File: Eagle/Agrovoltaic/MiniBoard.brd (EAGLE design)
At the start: 199.4 x 149.9 mm, 88 parts, among them J1 WAGO-03BE, J2 WAGO-03BE, J3 WAGO-03BE, K1 SRD-05VDC-SL-C, K3 SRD-05VDC-SL-C, Q1 BC338, Q2 BC338, U1 ESP32-DEVKIT-V1

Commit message: Revisi lagiii
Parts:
- removed LNC1, LNC2: (no value), led_WS:LED3MM
- removed R10, R15, R16, R9: (no value), rcl-ws:0309/12
- added A1: LM35DZ/NOPB, LM35DZ_NOPB:TO92127P521H735-3
- added PAD1, PAD10, PAD100, PAD101, PAD102, PAD103, PAD104, PAD11, PAD12, PAD13, PAD14, PAD15, PAD16, PAD17, PAD18, PAD19, PAD2, PAD20, PAD21, PAD22, PAD23, PAD24, PAD25, PAD26, PAD27, PAD28, PAD29, PAD3, PAD30, PAD31, PAD32, PAD33, PAD34, PAD35, PAD36, PAD37, PAD38, PAD39, PAD4, PAD40, PAD41, PAD42, PAD43, PAD44, PAD45, PAD46, PAD47, PAD48, PAD49, PAD5, PAD50, PAD51, PAD52, PAD53, PAD54, PAD55, PAD56, PAD57, PAD58, PAD59, PAD6, PAD60, PAD61, PAD62, PAD63, PAD64, PAD65, PAD66, PAD67, PAD68, PAD69, PAD7, PAD70, PAD71, PAD72, PAD73, PAD74, PAD75, PAD76, PAD77, PAD78, PAD79, PAD8, PAD80, PAD81, PAD82, PAD83, PAD84, PAD85, PAD86, PAD87, PAD88, PAD89, PAD9, PAD90, PAD91, PAD92, PAD93, PAD94, PAD95, PAD96, PAD97, PAD98, PAD99: WIREPAD1,6/0,9, wirepad-ws:1,6/0,9
- added RLM35: (no value), rcl-ws:0309/12
- moved R5 41.4 mm to (36.2, 125.6), turned to 90 degrees
- moved R3 41.1 mm to (5.97, 125.7), turned to 270 degrees
- moved RL5 2.62 mm to (193.7, 16.5)
- moved R4 2.07 mm to (60.6, 94.5)
- moved OLED_LCD 1.27 mm to (99.1, 63.5)
- moved R25 0.51 mm to (135.9, 99.8), turned to 180 degrees
- moved LNO1 0.51 mm to (7.62, 142.7), turned to 180 degrees
- moved LNO2 0.51 mm to (39.4, 142.7)
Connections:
- removed net N$11: LNC2.K, R16.1
- removed net N$13: LNC1.K, R10.1
- net 5V: now also A1.1
- net D25: now also A1.2, RLM35.2
- net GND: now also A1.3, R5.1, RLM35.1; no longer R10.2, R15.2, R16.2, R5.2, R9.2
- net N$10: now also R5.2; no longer R15.1
- net N$12: now also R3.1; no longer R9.1
- net N$3: now also LNO1.A; no longer R3.1
- net N$6: now also LNO2.A; no longer R5.1
- net NC1: no longer LNC1.A
- net NC2: no longer LNC2.A
- net NO1: no longer LNO1.A
- net NO2: no longer LNO2.A
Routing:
- net GND: track 1166.8 -> 1234.5 mm, vias 15 -> 12
- net N$6: track 35.4 -> 84.2 mm
- net S1: track 124.7 -> 165.1 mm
- net N$3: track 38.7 -> 60.6 mm
- net 5V: track 615.3 -> 593.7 mm, vias 8 -> 6
- net OUT1: track 32.7 -> 50.1 mm
- net D25: track 13.4 -> 26.8 mm
- net N$31: track 0.00 -> 12.3 mm
- net N$30: track 0.00 -> 12.3 mm
- net N$12: track 0.00 -> 11.7 mm
- net N$10: track 0.00 -> 11.6 mm
- net A1: track 208.2 -> 203.0 mm, vias 4 -> 3
- net OUT2: track 31.2 -> 35.9 mm
- net NC2: track 34.9 -> 30.5 mm
- net SCL: track 122.9 -> 126.4 mm
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
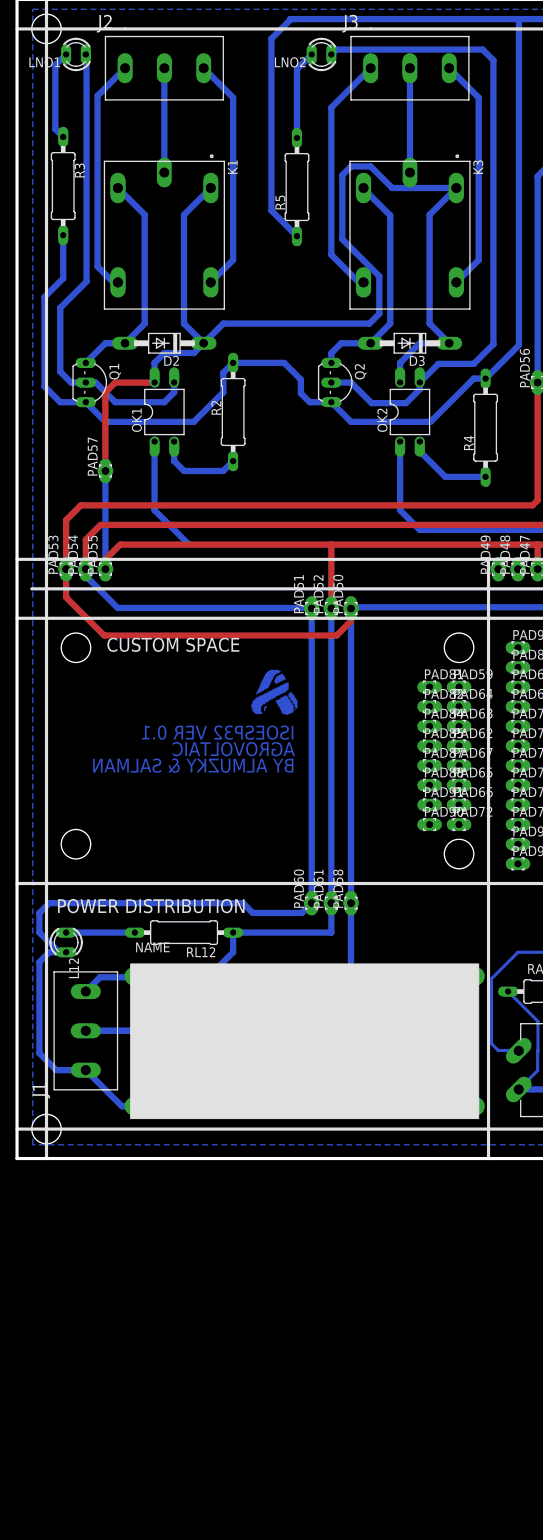
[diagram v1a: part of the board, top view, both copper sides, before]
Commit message: Revisi lagi lamp ke colector relay
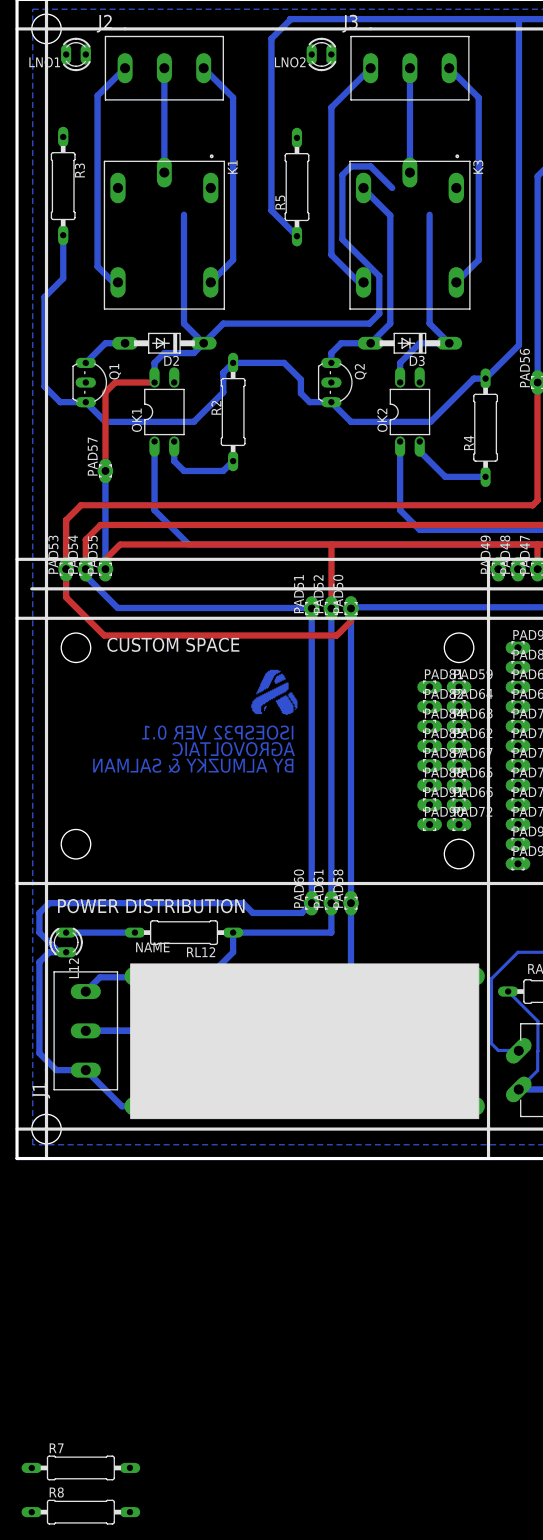
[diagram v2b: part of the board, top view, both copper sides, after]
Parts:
- added R7, R8: 2K, rcl-ws:0309/12
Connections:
- removed net N$12: LNO1.K, R3.1
- new net N$11: D2.A, K1.A2, LNO1.K, Q1.C
- net 12V: now also R7.1, R8.1
- net N$10: now also LNO1.A, R8.2; no longer LNO2.K, R5.2
- net N$3: now also R3.1; no longer LNO1.A
- net N$4: now also D3.A, K3.A2, LNO2.K, Q2.C; no longer D2.A, K1.A2, Q1.C
- net N$6: now also R5.2; no longer LNO2.A
- net N$7: now also LNO2.A, R7.2; no longer D3.A, K3.A2, Q2.C
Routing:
- net N$6: track 84.2 -> 0.00 mm
- net N$3: track 60.6 -> 0.00 mm
- net N$7: track 29.4 -> 0.00 mm
- net 12V: track 477.7 -> 459.6 mm
- net N$12: track 11.7 -> 0.00 mm
- net N$10: track 11.6 -> 0.00 mm
- net N$11: track 0.00 -> 6.13 mm
- net N$4: track 28.7 -> 29.3 mm

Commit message: Revisi board dan revisi wiring diagram
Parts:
- moved R8 178.1 mm to (19.1, 132.1), turned to 180 degrees
- moved R7 177.3 mm to (50.8, 132.1), turned to 180 degrees
- moved RA13 2.54 mm to (96.5, 110.5)
- moved R3 2.13 mm to (8.00, 125.1), turned to 90 degrees
- moved RA12 1.91 mm to (96.5, 117.5)
- moved RA22 1.91 mm to (76.2, 117.5)
- moved RA23 1.91 mm to (76.2, 111.1)
- moved R5 1.77 mm to (36.8, 124.0), turned to 270 degrees
- moved LNO2 0.90 mm to (40.0, 143.4)
- moved LNO1 0.90 mm to (8.26, 143.4)
- moved PAD56 0.64 mm to (67.3, 99.7)
- moved R26 0.64 mm to (119.4, 99.7)
- moved DZA1 0.63 mm to (95.2, 128.9)
- moved DZA3 0.63 mm to (77.5, 128.9)
- moved RA11 0.63 mm to (96.5, 123.8)
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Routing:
- net 12V: track 459.6 -> 550.7 mm
- net N$11: track 6.13 -> 79.5 mm
- net N$4: track 29.3 -> 75.5 mm
- net N$3: track 0.00 -> 35.2 mm
- net N$6: track 0.00 -> 33.7 mm
- net N$10: track 0.00 -> 23.0 mm
- net N$7: track 0.00 -> 21.7 mm
- net 5V: track 593.7 -> 610.6 mm
- net GND: track 1234.5 -> 1230.0 mm
- net AI1: track 31.2 -> 32.1 mm
- net A2: track 234.8 -> 234.1 mm
- net A1: track 203.0 -> 202.4 mm
- net NO1: track 30.6 -> 31.1 mm
- net AI2: track 41.6 -> 42.1 mm

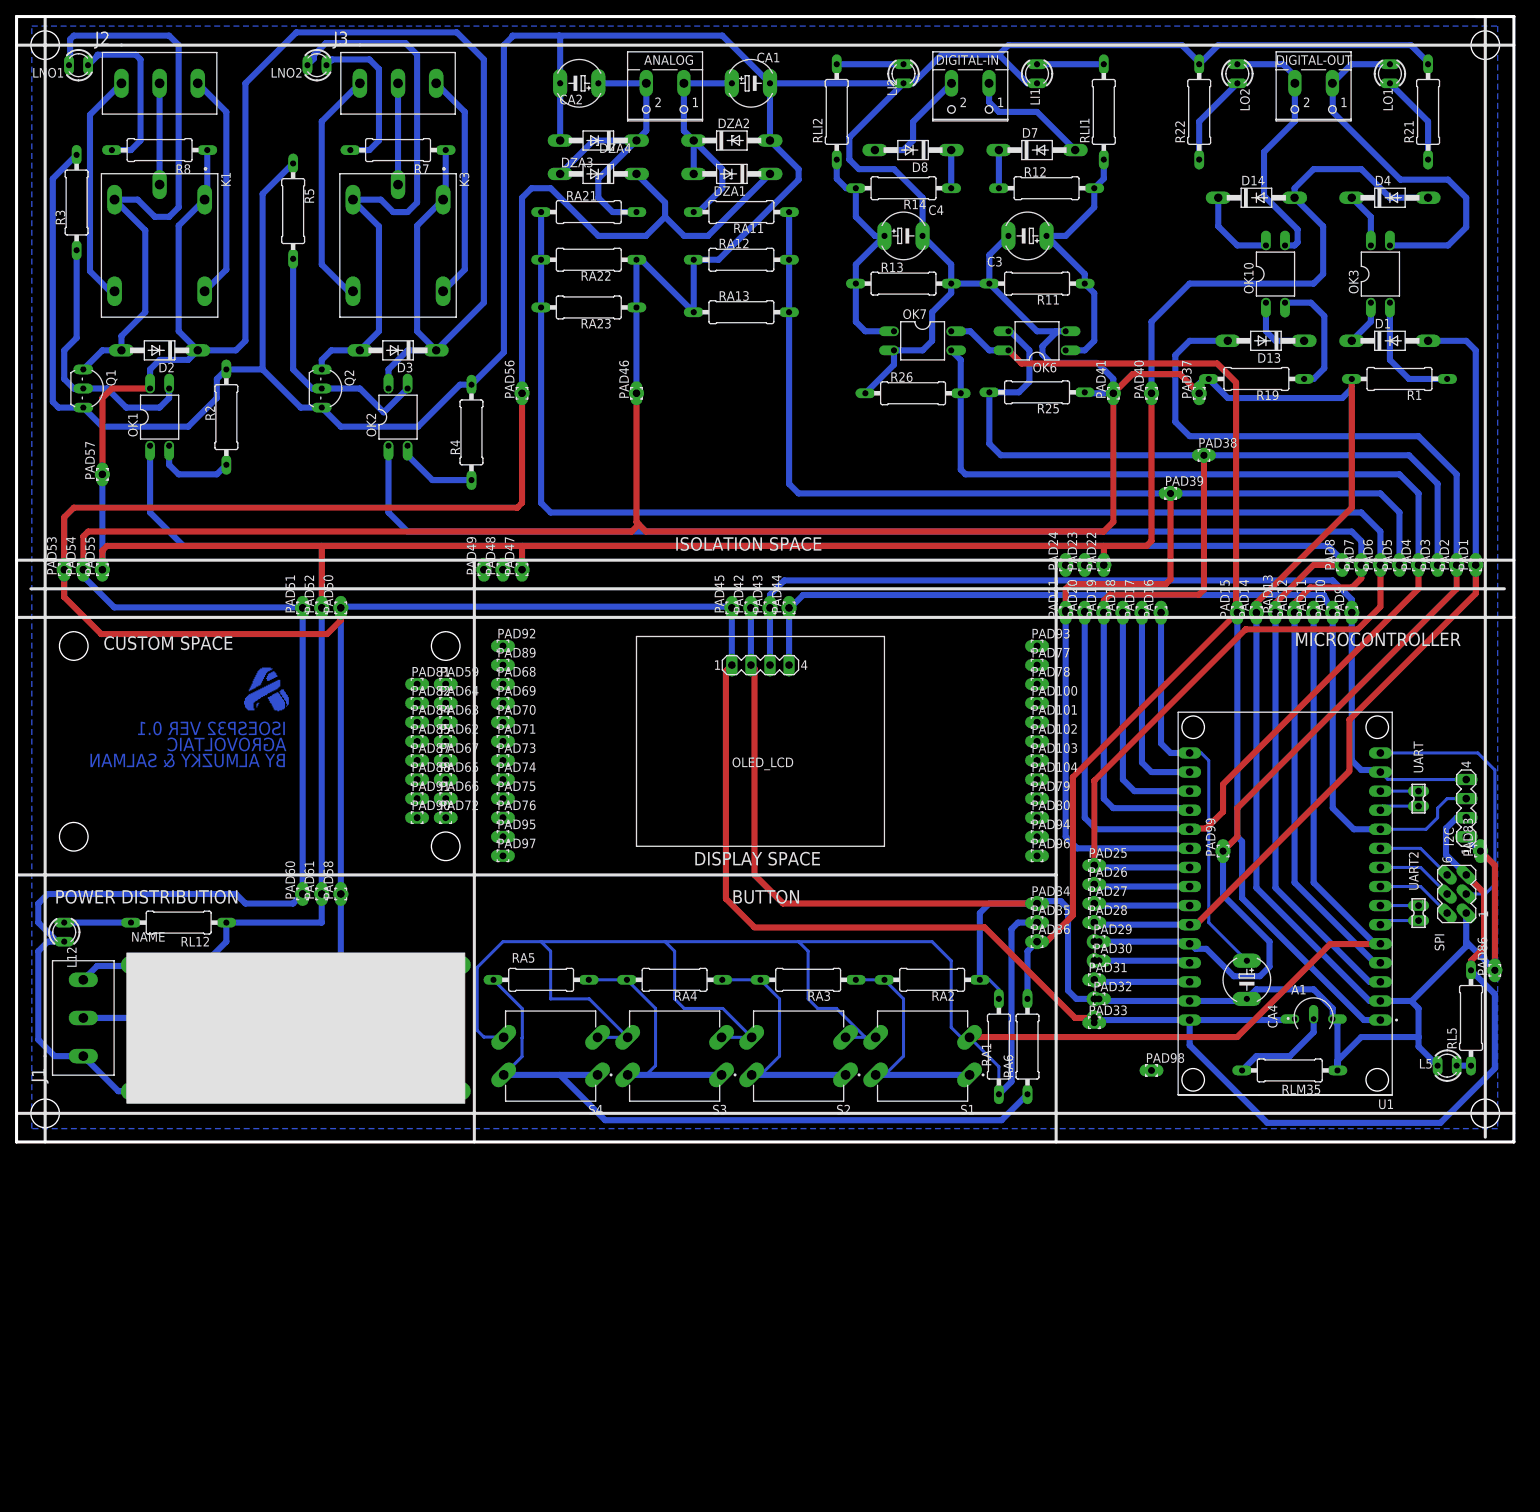
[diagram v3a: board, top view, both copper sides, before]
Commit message: ADD:Menambahkan pembacaan data
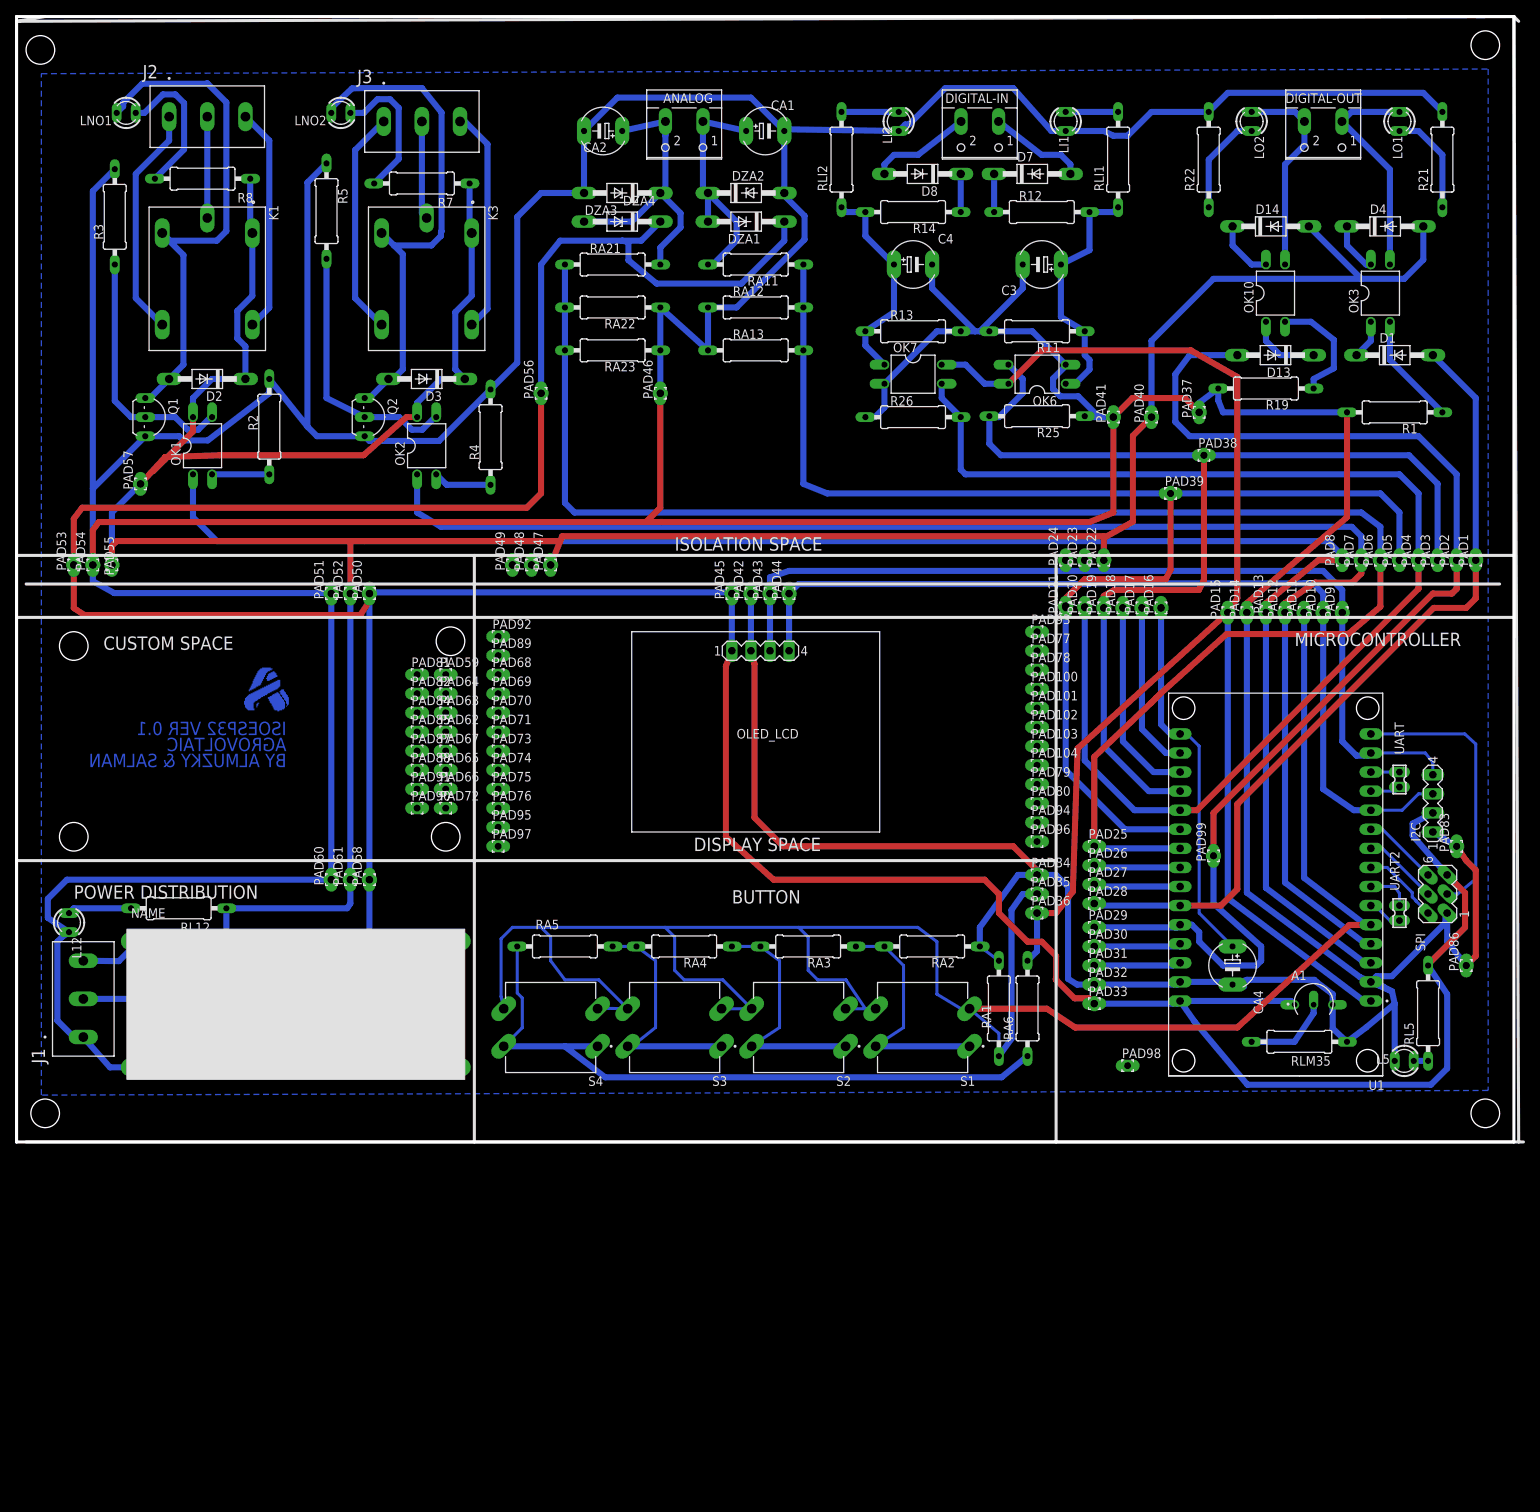
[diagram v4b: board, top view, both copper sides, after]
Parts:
- moved Q1 9.09 mm to (18.4, 96.5)
- moved LNO1 8.98 mm to (14.6, 137.0)
- moved J2 7.75 mm to (20.3, 136.5)
- moved K1 7.75 mm to (25.4, 114.9)
- moved DZA4 7.67 mm to (80.6, 126.4)
- moved RA21 7.67 mm to (79.4, 116.8)
- moved LI1 7.41 mm to (139.7, 135.9)
- moved D2 7.41 mm to (25.4, 101.6)
- moved DZA2 7.24 mm to (97.2, 126.4)
- moved RA11 7.24 mm to (98.4, 116.8)
- moved LNO2 7.10 mm to (43.2, 137.0)
- moved CA2 7.10 mm to (78.1, 134.6)
- moved DZA3 7.10 mm to (80.6, 122.6)
- moved RA22 7.10 mm to (79.4, 111.1)
- moved Q2 6.87 mm to (47.6, 96.5)
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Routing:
- net 12V: track 550.7 -> 454.5 mm, vias 7 -> 8
- net GND: track 1230.0 -> 1164.6 mm
- net 5V: track 610.6 -> 561.3 mm
- net OUT1: track 50.1 -> 29.9 mm
- net D4: track 304.6 -> 284.8 mm
- net A1: track 202.4 -> 183.8 mm
- net S1: track 165.1 -> 149.9 mm
- net A2: track 234.1 -> 221.8 mm
- net S2: track 179.6 -> 167.6 mm
- net SDA: track 132.2 -> 121.6 mm
- net RR1: track 239.4 -> 229.3 mm
- net N$11: track 79.5 -> 70.3 mm
- net RR2: track 208.7 -> 200.2 mm
- net N$4: track 75.5 -> 67.1 mm
- net OUT2: track 35.9 -> 27.7 mm
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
